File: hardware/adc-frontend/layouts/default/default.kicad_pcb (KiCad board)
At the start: 2 copper layers, 0 parts

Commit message: main.ato改修完了: オフラインato buildでPCB/BOM/ネットリスト生成成功
atopile部品API停止下で、EasyEDA取り込み部品を使い完全オフラインで
ato buildを通した。成果物: default.kicad_pcb(104フットプリント/612ネット)、
default.bom.csv(LCSC番号付き発注可能BOM)。

- parts/_mech/mech.ato: 手実装機構部品(ヘッダ2x15/1x4・ソルダージャンパ・
  TOSLINK PLR135)をフットプリント同居ディレクトリに配置し is_atomic_part +
  has_part_removed(DNP: 基板にFPは載るがJLC発注除外)で定義。自作footprint/symbol生成
- コネクタ(usbc/jack)のmanufacturer不一致修正
- EsdArray4をROHM EMZT6.8ET2R(6ピンA-Common Quad)へ

既知の残課題(製造前): (1)pinoutドキュメント生成はMagJack等のシンボル/パッド
不一致で失敗(netlist/PCBは生成済み)。(2)コネクタ類の仮ピン番号は実部品/EXT基板と
要照合。(3)ESD共通ノード位置(pin2/5)をROHMデータシートで要確認。(4)BOM値表示が
シンボリック({ℝ+}F)だがLCSC番号で部品は確定。

Co-Authored-By: Claude Fable 5 <noreply@anthropic.com>
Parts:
- added C1: {ℝ+}F, SAMSUNG_CL10A105KB8NNNC:C0603, F.Cu at (720.0, 0.00)
- added C10: {ℝ+}F, SAMSUNG_CL05B104KO5NNNC:C0402, F.Cu at (840.0, 0.00)
- added C11: {ℝ+}F, SAMSUNG_CL05B104KO5NNNC:C0402, F.Cu at (850.0, 0.00)
- added C12: {ℝ+}F, SAMSUNG_CL05B104KO5NNNC:C0402, F.Cu at (860.0, 0.00)
- added C13: {ℝ+}F, SAMSUNG_CL21A106KAYNNNE:C0805, F.Cu at (700.0, 0.00)
- added C14: {ℝ+}F, SAMSUNG_CL05B104KO5NNNC:C0402, F.Cu at (470.0, 0.00)
- added C15: {ℝ+}F, SAMSUNG_CL05B104KO5NNNC:C0402, F.Cu at (490.0, 0.00)
- added C16: {ℝ+}F, FH_0402B472K500NT:C0402, F.Cu at (500.0, 0.00)
- added C17: {ℝ+}F, SAMSUNG_CL05B104KO5NNNC:C0402, F.Cu at (510.0, 0.00)
- added C18: {ℝ+}F, FH_0402B102K500NT:C0402, F.Cu at (430.0, 0.00)
- added C19: {ℝ+}F, SAMSUNG_CL05B104KO5NNNC:C0402, F.Cu at (900.0, 0.00)
- added C2: {ℝ+}F, SAMSUNG_CL10A105KB8NNNC:C0603, F.Cu at (730.0, 0.00)
- added C20: {ℝ+}F, FH_0402B102K500NT:C0402, F.Cu at (460.0, 0.00)
- added C21: {ℝ+}F, SAMSUNG_CL05B104KO5NNNC:C0402, F.Cu at (680.0, 0.00)
- added C22: {ℝ+}F, SAMSUNG_CL05B104KO5NNNC:C0402, F.Cu at (410.0, 0.00)
- added C23: {ℝ+}F, SAMSUNG_CL05B104KO5NNNC:C0402, F.Cu at (390.0, 0.00)
- added C24: {ℝ+}F, SAMSUNG_CL05B104KO5NNNC:C0402, F.Cu at (370.0, 0.00)
- added C25: {ℝ+}F, SAMSUNG_CL05B104KO5NNNC:C0402, F.Cu at (220.0, 0.00)
- added C26: {ℝ+}F, SAMSUNG_CL05B104KO5NNNC:C0402, F.Cu at (230.0, 0.00)
- added C27: {ℝ+}F, SAMSUNG_CL05B104KO5NNNC:C0402, F.Cu at (240.0, 0.00)
- added C28: {ℝ+}F, SAMSUNG_CL05B104KO5NNNC:C0402, F.Cu at (250.0, 0.00)
- added C29: {ℝ+}F, SAMSUNG_CL05B104KO5NNNC:C0402, F.Cu at (260.0, 0.00)
- added C3: {ℝ+}F, SAMSUNG_CL21A106KAYNNNE:C0805, F.Cu at (740.0, 0.00)
- added C30: {ℝ+}F, SAMSUNG_CL05B104KO5NNNC:C0402, F.Cu at (270.0, 0.00)
- added C31: {ℝ+}F, SAMSUNG_CL05B104KO5NNNC:C0402, F.Cu at (280.0, 0.00)
- added C32: {ℝ+}F, SAMSUNG_CL05B104KO5NNNC:C0402, F.Cu at (290.0, 0.00)
- added C33: {ℝ+}F, SAMSUNG_CL05B104KO5NNNC:C0402, F.Cu at (300.0, 0.00)
- added C34: {ℝ+}F, SAMSUNG_CL05B104KO5NNNC:C0402, F.Cu at (310.0, 0.00)
- added C35: {ℝ+}F, SAMSUNG_CL05B104KO5NNNC:C0402, F.Cu at (320.0, 0.00)
- added C36: {ℝ+}F, SAMSUNG_CL05B104KO5NNNC:C0402, F.Cu at (330.0, 0.00)
- added C37: {ℝ+}F, SAMSUNG_CL05B104KO5NNNC:C0402, F.Cu at (340.0, 0.00)
- added C38: {ℝ+}F, SAMSUNG_CL05B104KO5NNNC:C0402, F.Cu at (350.0, 0.00)
- added C39: {ℝ+}F, SAMSUNG_CL05B104KO5NNNC:C0402, F.Cu at (940.0, 0.00)
- added C4: {ℝ+}F, SAMSUNG_CL05B104KO5NNNC:C0402, F.Cu at (750.0, 0.00)
- added C40: {ℝ+}F, SAMSUNG_CL05B104KO5NNNC:C0402, F.Cu at (950.0, 0.00)
- added C41: {ℝ+}F, YAGEO_CC1812KKX7RDBB472:C1812, F.Cu at (1020.0, 0.00)
- added C42: {ℝ+}F, YAGEO_CC1812KKX7RDBB472:C1812, F.Cu at (1030.0, 0.00)
- added C43: {ℝ+}F, SAMSUNG_CL05B104KO5NNNC:C0402, F.Cu at (980.0, 0.00)
- added C44: {ℝ+}F, SAMSUNG_CL05B104KO5NNNC:C0402, F.Cu at (990.0, 0.00)
- added C45: {ℝ+}F, SAMSUNG_CL05B104KO5NNNC:C0402, F.Cu at (1000.0, 0.00)
- added C46: {ℝ+}F, SAMSUNG_CL05B104KO5NNNC:C0402, F.Cu at (1010.0, 0.00)
- added C47: {ℝ+}F, SAMSUNG_CL05B103KB5NNNC:C0402, F.Cu at (520.0, 0.00)
- added C48: {ℝ+}F, SAMSUNG_CL05B103KB5NNNC:C0402, F.Cu at (530.0, 0.00)
- added C49: {ℝ+}F, SAMSUNG_CL05B103KB5NNNC:C0402, F.Cu at (540.0, 0.00)
- added C5: {ℝ+}F, SAMSUNG_CL05B104KO5NNNC:C0402, F.Cu at (760.0, 0.00)
- added C50: {ℝ+}F, SAMSUNG_CL05B103KB5NNNC:C0402, F.Cu at (550.0, 0.00)
- added C51: {ℝ+}F, SAMSUNG_CL05B103KB5NNNC:C0402, F.Cu at (560.0, 0.00)
- added C52: {ℝ+}F, SAMSUNG_CL05B103KB5NNNC:C0402, F.Cu at (570.0, 0.00)
- added C53: {ℝ+}F, SAMSUNG_CL05B103KB5NNNC:C0402, F.Cu at (580.0, 0.00)
- added C54: {ℝ+}F, FH_0402B102K500NT:C0402, F.Cu at (590.0, 0.00)
- added C55: {ℝ+}F, FH_0402B102K500NT:C0402, F.Cu at (600.0, 0.00)
- added C56: {ℝ+}F, SAMSUNG_CL21A106KAYNNNE:C0805, F.Cu at (110.0, 0.00)
- added C57: {ℝ+}F, SAMSUNG_CL21A106KAYNNNE:C0805, F.Cu at (120.0, 0.00)
- added C58: {ℝ+}F, SAMSUNG_CL21A106KAYNNNE:C0805, F.Cu at (130.0, 0.00)
- added C59: {ℝ+}F, SAMSUNG_CL21A106KAYNNNE:C0805, F.Cu at (140.0, 0.00)
- added C6: {ℝ+}F, SAMSUNG_CL05B104KO5NNNC:C0402, F.Cu at (770.0, 0.00)
- added C60: {ℝ+}F, SAMSUNG_CL21A106KAYNNNE:C0805, F.Cu at (150.0, 0.00)
- added C7: {ℝ+}F, SAMSUNG_CL10A105KB8NNNC:C0603, F.Cu at (810.0, 0.00)
- added C8: {ℝ+}F, SAMSUNG_CL10A105KB8NNNC:C0603, F.Cu at (820.0, 0.00)
- added C9: {ℝ+}F, SAMSUNG_CL21A106KAYNNNE:C0805, F.Cu at (830.0, 0.00)
- added D1: , ROHM_EMZT6_8ET2R:EMT6_L1.6-W1.2-P0.50-LS1.6-BL, F.Cu at (880.0, 0.00)
- added D2: , ROHM_EMZT6_8ET2R:EMT6_L1.6-W1.2-P0.50-LS1.6-BL, F.Cu at (420.0, 0.00)
- added D3: , ROHM_EMZT6_8ET2R:EMT6_L1.6-W1.2-P0.50-LS1.6-BL, F.Cu at (440.0, 0.00)
- added FB1: , TDK_MPZ1608S221ATA00:L0603, F.Cu at (690.0, 0.00)
- added FB2: , TDK_MPZ1608S221ATA00:L0603, F.Cu at (200.0, 0.00)
- added FB3: , TDK_MPZ1608S221ATA00:L0603, F.Cu at (210.0, 0.00)
- added J1: , _mech:Header_2x15_P2.54mm, F.Cu at (960.0, 0.00)
- added J10: , BOOMELE_VGA_002:D-SUB-TH_VGA-002, F.Cu at (10.0, 0.00)
- added J2: , HANRUN_HR911130A:RJ45-TH_HR911130A, F.Cu at (970.0, 0.00)
- added J3: , _mech:Header_2x15_P2.54mm, F.Cu at (650.0, 0.00)
- added J4: , _mech:Header_2x15_P2.54mm, F.Cu at (660.0, 0.00)
- added J5: , _mech:Header_1x4_P2.54mm, F.Cu at (910.0, 0.00)
- added J6: , UNKNOWN_PJ_327C_4A:AUDIO-SMD_PJ-327C-4A, F.Cu at (870.0, 0.00)
- added J7: , SHOU_HAN_DC005:DC-IN-TH_DC005, F.Cu at (40.0, 0.00)
- added J8: , _mech:PLR135_T10, F.Cu at (890.0, 0.00)
- added J9: , UNKNOWN_TYPE_C_31_M_12:USB-C_SMD-TYPE-C-31-M-12_1, F.Cu at (160.0, 0.00)
- added JP1: , _mech:SolderJumper_2, F.Cu at (780.0, 0.00)
- added JP2: , _mech:SolderJumper_2, F.Cu at (790.0, 0.00)
- added JP3: , _mech:SolderJumper_2, F.Cu at (190.0, 0.00)
- added R1: {ℝ+}Ω, UNI_ROYAL_0402WGF750JTCE:R0402, F.Cu at (400.0, 0.00)
- added R10: {ℝ+}Ω, UNI_ROYAL_0402WGF2201TCE:R0402, F.Cu at (620.0, 0.00)
- added R11: {ℝ+}Ω, UNI_ROYAL_0402WGF2200TCE:R0402, F.Cu at (450.0, 0.00)
- added R12: {ℝ+}Ω, FOJAN_FRC0402F62R0TS:R0402, F.Cu at (100.0, 0.00)
- added R13: {ℝ+}Ω, UNI_ROYAL_0402WGF1200TCE:R0402, F.Cu at (90.0, 0.00)
- added R2: {ℝ+}Ω, UNI_ROYAL_0402WGF750JTCE:R0402, F.Cu at (380.0, 0.00)
- added R3: {ℝ+}Ω, UNI_ROYAL_0402WGF750JTCE:R0402, F.Cu at (360.0, 0.00)
- added R4: {ℝ+}Ω, UNI_ROYAL_0402WGF5101TCE:R0402, F.Cu at (170.0, 0.00)
- added R5: {ℝ+}Ω, UNI_ROYAL_0402WGF5101TCE:R0402, F.Cu at (180.0, 0.00)
- added R6: {ℝ+}Ω, UNI_ROYAL_0402WGF1501TCE:R0402, F.Cu at (480.0, 0.00)
- added R7: {ℝ+}Ω, UNI_ROYAL_0402WGF2201TCE:R0402, F.Cu at (610.0, 0.00)
- added R8: {ℝ+}Ω, UNI_ROYAL_0402WGF2201TCE:R0402, F.Cu at (640.0, 0.00)
- added R9: {ℝ+}Ω, UNI_ROYAL_0402WGF2201TCE:R0402, F.Cu at (630.0, 0.00)
- added U1: , TI_PCM1808PWR:TSSOP-14_L5.0-W4.4-P0.65-LS6.4-BL, F.Cu at (710.0, 0.00)
- added U10: , TI_TVP7002PZP:HTQFP-100_L14.0-W14.0-P0.50-LS16.0-BL-EP6.2, F.Cu at (0.00, 0.00)
- added U2: , TI_PCM1808PWR:TSSOP-14_L5.0-W4.4-P0.65-LS6.4-BL, F.Cu at (800.0, 0.00)
- added U3: , TI_SN74LVC2G17DBVR:SOT-23-6_L2.9-W1.6-P0.95-LS2.8-BL, F.Cu at (20.0, 0.00)
- added U4: , MICROCHIP_24AA025E48_I_SN:SOIC-8_L4.9-W3.9-P1.27-LS6.0-BL, F.Cu at (920.0, 0.00)
- added U5: , MICROCHIP_24AA025E48_I_SN:SOIC-8_L4.9-W3.9-P1.27-LS6.0-BL, F.Cu at (930.0, 0.00)
- added U6: , DIODES_AZ1117H_ADJTRE1:SOT-223-3_L6.5-W3.4-P2.30-LS7.0-BR, F.Cu at (70.0, 0.00)
- added U7: , DIODES_AZ1117H_3_3TRE1:SOT-223-3_L6.5-W3.4-P2.30-LS7.0-BR, F.Cu at (60.0, 0.00)
- added U8: , TI_TLV70019DDCR:SOT-23-5_L2.9-W1.6-P0.95-LS2.8-BR, F.Cu at (80.0, 0.00)
- added U9: , DIODES_AZ1117H_3_3TRE1:SOT-223-3_L6.5-W3.4-P2.30-LS7.0-BR, F.Cu at (50.0, 0.00)
- added X1: , YXC_X322527MSB4SI:CRYSTAL-SMD_4P-L3.2-W2.5-BL-1, F.Cu at (30.0, 0.00)
- added X2: , YXC_OT2JI_111_12_288M:OSC-SMD_4P-L3.2-W2.5-BL, F.Cu at (670.0, 0.00)

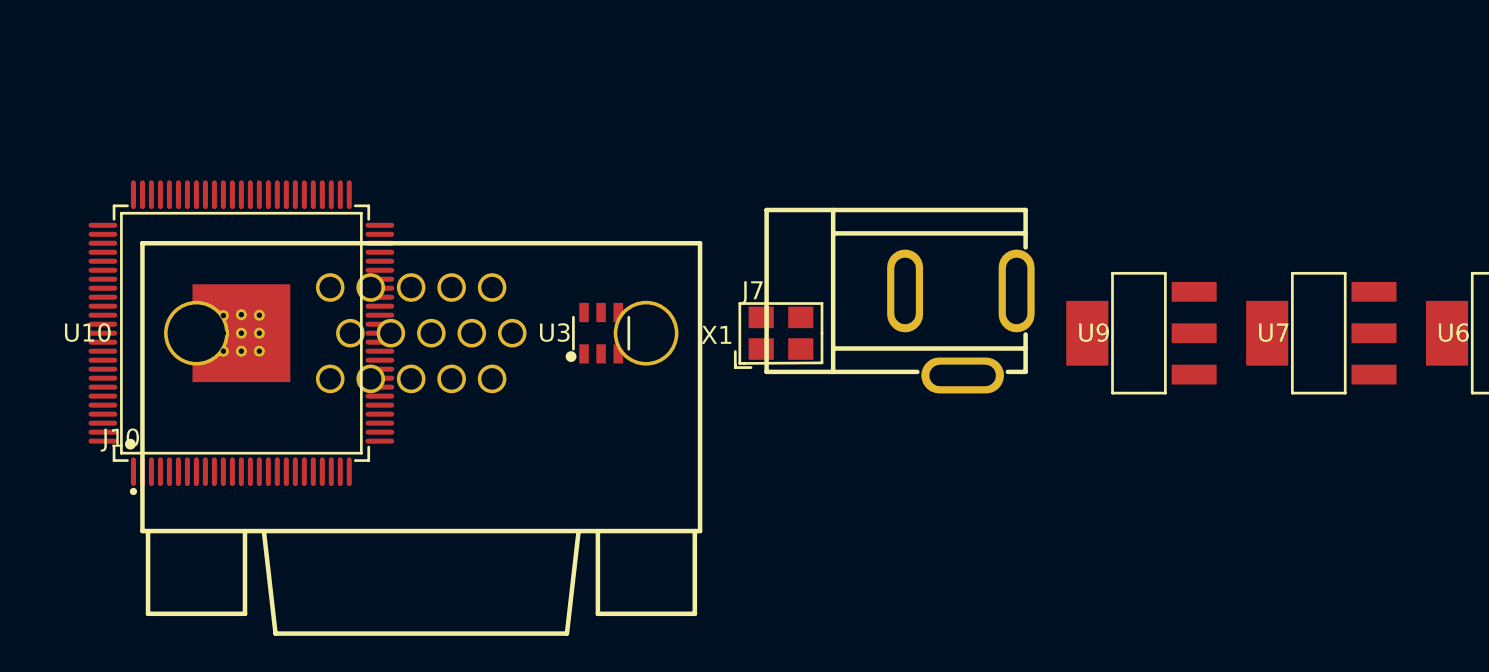
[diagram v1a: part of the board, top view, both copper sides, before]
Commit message: VGAを日本式D-SUB15(2列/X68000ピン配置)へ変更
3列HD-15(VGA-002)を廃し、2列DA-15メス CONNFLY DS1037-15FNAKT76-0CC
(C77836、EasyEDA取り込み)へ。X68000ピン配置(ohnaka提供):
1R 2RGND 3G 4GGND 5B 6BGND 7YS 8GND 9NC 10AudioL 11AudioR 12GND 13NC 14HSync 15VSync。
- RGB各GNDが交互配置。音声はpin10/11から取得(旧: VGA DDCピンの仮タップを廃止)
- 同期はpin14/15。YS(pin7)は未使用、pin9/13はNC
- App配線をr/g/b/audio_l/audio_r/hsync/vsync/*_gndへ再マッピング
オフラインato build確認(BOMにJ10=DS1037-15F)。VGA-002 partは未参照(残置)。

Co-Authored-By: Claude Fable 5 <noreply@anthropic.com>
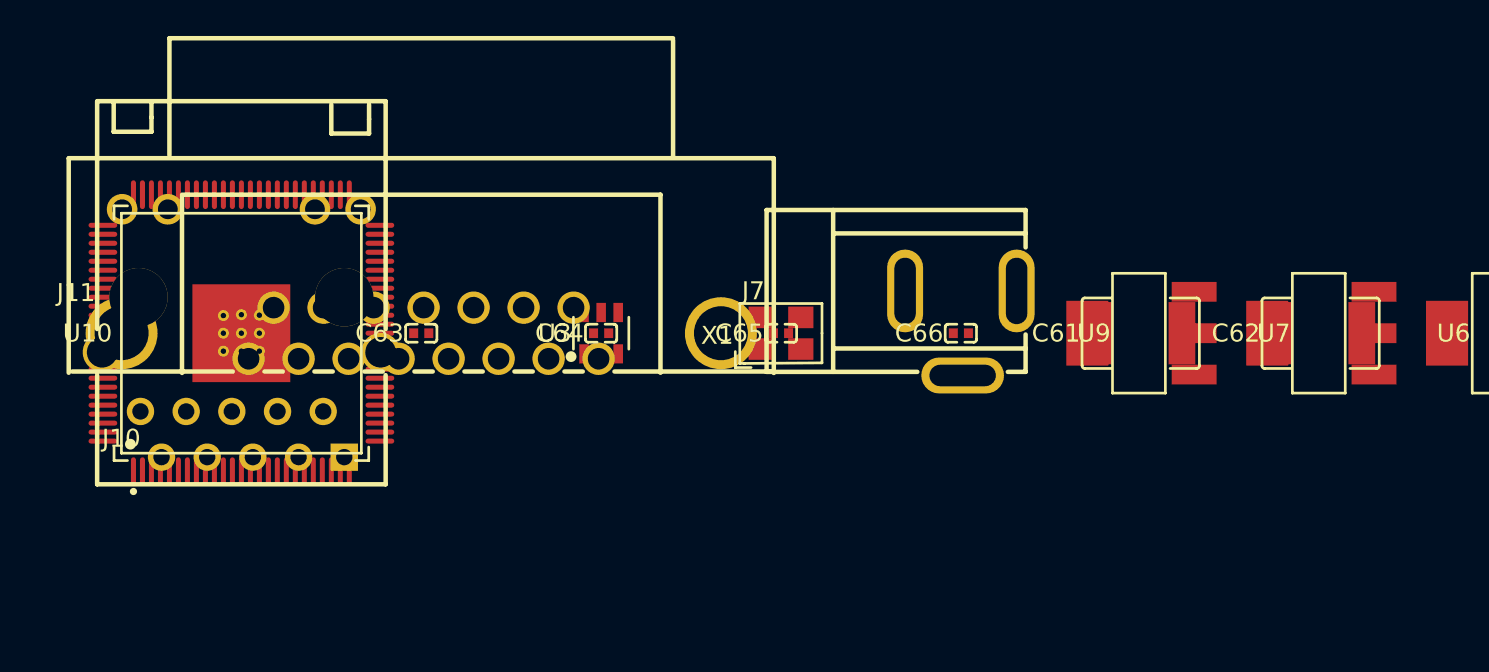
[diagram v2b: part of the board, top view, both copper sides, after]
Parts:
- added C61: {ℝ+}F, YAGEO_CC1812KKX7RDBB472:C1812, F.Cu at (50.0, 0.00)
- added C62: {ℝ+}F, YAGEO_CC1812KKX7RDBB472:C1812, F.Cu at (60.0, 0.00)
- added C63: {ℝ+}F, SAMSUNG_CL05B104KO5NNNC:C0402, F.Cu at (10.0, 0.00)
- added C64: {ℝ+}F, SAMSUNG_CL05B104KO5NNNC:C0402, F.Cu at (20.0, 0.00)
- added C65: {ℝ+}F, SAMSUNG_CL05B104KO5NNNC:C0402, F.Cu at (30.0, 0.00)
- added C66: {ℝ+}F, SAMSUNG_CL05B104KO5NNNC:C0402, F.Cu at (40.0, 0.00)
- added J11: , HANRUN_HR911130A:RJ45-TH_HR911130A, F.Cu at (0.00, 0.00)
- J10: footprint BOOMELE_VGA_002:D-SUB-TH_VGA-002 -> CONNFLY_DS1037_15FNAKT76_0CC:DSUB-TH_DS1037-15FNAKT74-0CC
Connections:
- J10 pad 1: c_ac-power-hv-1 -> (no net)
- J10 pad 10: gnd -> (no net)
- J10 pad 11: a-1 -> (no net)
- J10 pad 12: vga-sda -> (no net)
- J10 pad 13: 1 -> (no net)
- J10 pad 14: vsync -> (no net)
- J10 pad 15: vga-scl -> (no net)
- J10 pad 16: gnd -> (no net)
- J10 pad 2: c_sog3-power-hv -> (no net)
- J10 pad 3: c_ac-power-hv -> (no net)
- J10 pad 4: a -> (no net)
- J10 pad 5: gnd -> (no net)
- J10 pad 6: gnd -> (no net)
- J10 pad 7: gnd -> (no net)
- J10 pad 8: gnd -> (no net)
- J10 pad 9: key -> (no net)

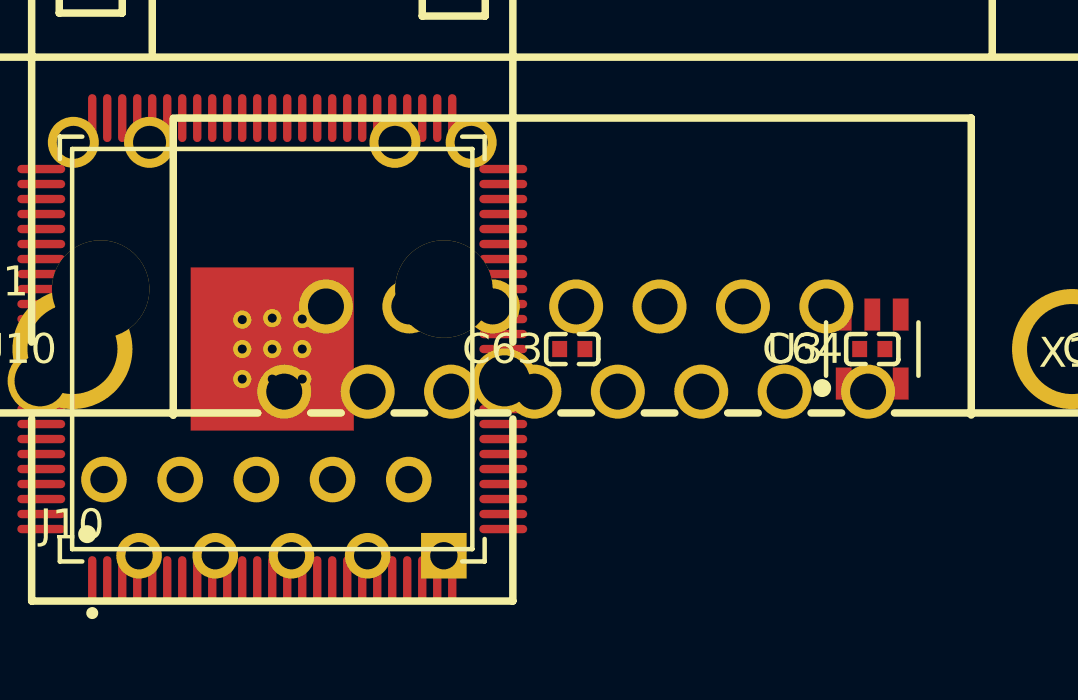
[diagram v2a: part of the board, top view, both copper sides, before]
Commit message: ArgusX接続用 2x8ボックスヘッダを追加(代替映像入力)
別プロジェクトArgusX(アナログRGBマトリクスセレクタ)の2x8汎用映像端子
(docs/design.md 3.1)と嵌合するボックスヘッダをRetroCastXに追加。
- ピン割当をArgusXに一致: 1R 2GND 3G 4GND 5B 6GND 7音声L 8音声R 9GND
  10H(TTL/CSYNC) 11V(TTL) 12GND 13+5V 14GND 15VBUS 16GND
- D-SUB15と同じ前段ノード(ESD+75Ω終端+ACカップリング/同期/音声)へ並列接続。
  使用は排他(同時に片方のみ)。電源13/15は両基板自己給電のため未接続
- 2x8シュラウド付きボックスヘッダのフットプリント+シンボルを自作(手実装/DNP)
オフラインato build確認(フットプリント111→112)。

Co-Authored-By: Claude Fable 5 <noreply@anthropic.com>
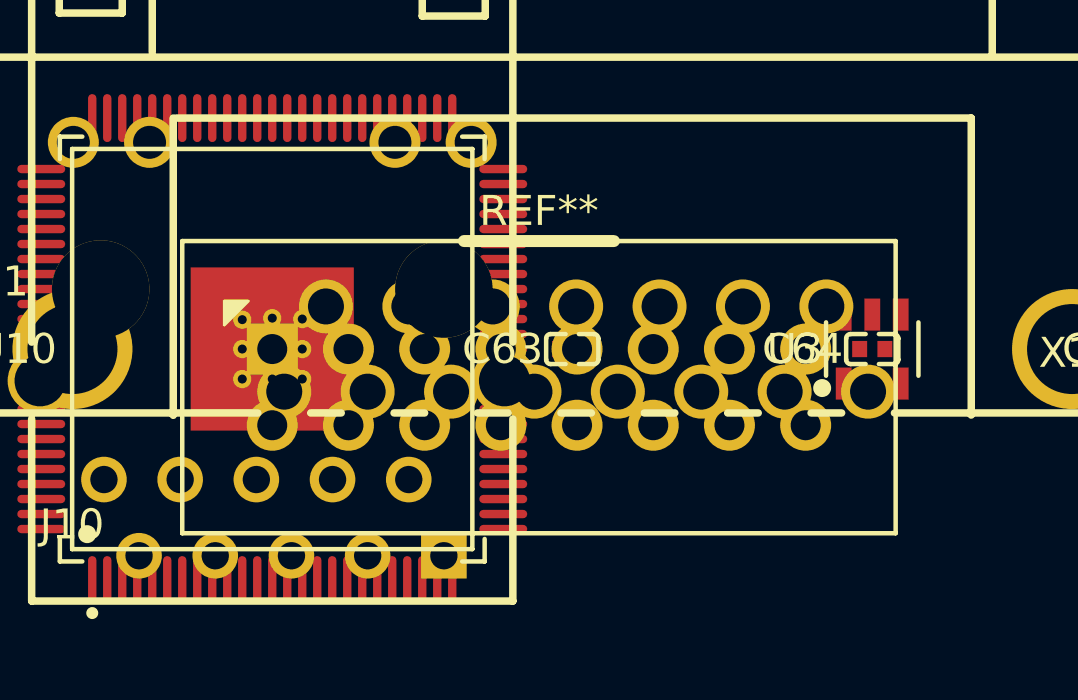
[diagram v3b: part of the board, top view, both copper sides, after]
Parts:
- added J12: , _mech:BoxHeader_2x8_P2.54mm, F.Cu at (0.00, 0.00)
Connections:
- C22 pad 1: c_ac-power-hv -> c_ac-power-hv-1
- C24 pad 1: c_ac-power-hv-1 -> c_ac-power-hv
- D2 pad 1: c_ac-power-hv-1 -> c_ac-power-hv
- D2 pad 4: c_ac-power-hv -> c_ac-power-hv-1
- D3 pad 1: 1 -> hsync
- J1 pad 1: eth.j8-1 -> 1
- J1 pad 19: eth.j8-1 -> 1
- J1 pad 2: eth.j8-1 -> 1
- J1 pad 20: eth.j8-1 -> 1
- J10 pad 1: (no net) -> c_ac-power-hv
- J10 pad 10: (no net) -> audio_l
- J10 pad 11: (no net) -> audio_r
- J10 pad 12: (no net) -> gnd
- J10 pad 14: (no net) -> hsync
- J10 pad 15: (no net) -> vsync
- J10 pad 16: (no net) -> gnd
- J10 pad 17: (no net) -> gnd
- J10 pad 2: (no net) -> gnd
- J10 pad 3: (no net) -> c_sog3-power-hv
- J10 pad 4: (no net) -> gnd
- J10 pad 5: (no net) -> c_ac-power-hv-1
- J10 pad 6: (no net) -> gnd
- J10 pad 7: (no net) -> ys
- J10 pad 8: (no net) -> gnd
- JP1 pad 1: a -> audio_l
- JP2 pad 1: a-1 -> audio_r
- R1 pad 1: c_ac-power-hv -> c_ac-power-hv-1
- R3 pad 1: c_ac-power-hv-1 -> c_ac-power-hv
- U3 pad 1: 1 -> hsync

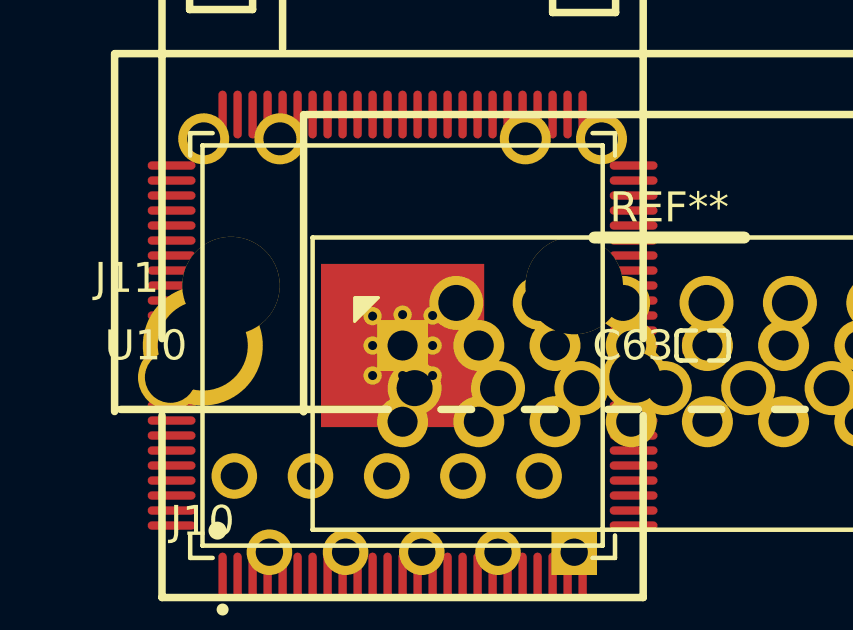
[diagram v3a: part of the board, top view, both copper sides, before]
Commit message: YS信号(D-SUB15 pin7)のテストパッドを追加
X68000のYSはスーパーインポーズ/イメージユニット関連のstatus信号らしい
(確定情報は未取得、capture用途では不要)。将来取り込む場合に備え、
1穴THテストパッド(Tp1Pad)へ引き出してNG時に配線可能にした。

実装メモ:
- コンポーネント名は標準ライブラリのTestPointと衝突するためTp1Padに改名
- テストパッドのフットプリントはfp_circleがあると"min() empty"で
  Updating PCBが落ちるため、パッドのみの最小構成にした
オフラインato build確認(フットプリント112→113、bom通過)。

Co-Authored-By: Claude Fable 5 <noreply@anthropic.com>
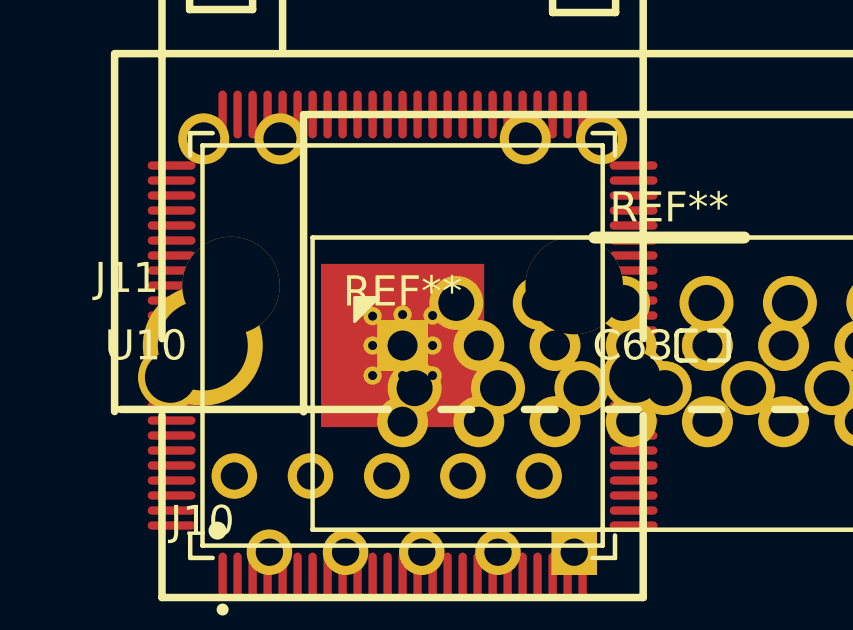
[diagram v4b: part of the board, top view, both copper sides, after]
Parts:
- added TP1: , _mech:TestPoint_TH1, F.Cu at (0.00, 0.00)
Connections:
- J10 pad 7: ys -> pad
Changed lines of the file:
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@@
 	(net 136 "audio_r")
 	(net 137 "audio_l")
-	(net 138 "ys")
+	(net 22 "pad")
 	(footprint "TI_TVP7002PZP:HTQFP-100_L14.0-W14.0-P0.50-LS16.0-BL-EP6.2"
 		(layer "F.Cu")
@@
 			(drill 1.199896)
 			(layers "*.Cu" "*.Mask")
-			(net 138 "ys")
+			(net 22 "pad")
 		)
 		(pad "8" thru_hole circle
@@
 		)
 		(pad "1" thru_hole rect
-			(at 0 0 0)
+			(at 0 0)
 			(size 1.7 1.7)
 			(drill 1)
@@
 		)
 		(pad "2" thru_hole oval
-			(at 0 2.54 0)
+			(at 0 2.54)
 			(size 1.7 1.7)
 			(drill 1)
@@
 		)
 		(pad "3" thru_hole oval
-			(at 2.54 0 0)
+			(at 2.54 0)
 			(size 1.7 1.7)
 			(drill 1)
@@
 		)
 		(pad "4" thru_hole oval
-			(at 2.54 2.54 0)
+			(at 2.54 2.54)
 			(size 1.7 1.7)
 			(drill 1)
@@
 		)
 		(pad "5" thru_hole oval
-			(at 5.08 0 0)
+			(at 5.08 0)
 			(size 1.7 1.7)
 			(drill 1)
@@
 		)
 		(pad "6" thru_hole oval
-			(at 5.08 2.54 0)
+			(at 5.08 2.54)
 			(size 1.7 1.7)
 			(drill 1)
@@
 		)
 		(pad "7" thru_hole oval
-			(at 7.62 0 0)
+			(at 7.62 0)
 			(size 1.7 1.7)
 			(drill 1)
@@
 		)
 		(pad "8" thru_hole oval
-			(at 7.62 2.54 0)
+			(at 7.62 2.54)
 			(size 1.7 1.7)
 			(drill 1)
@@
 		)
 		(pad "9" thru_hole oval
-			(at 10.16 0 0)
+			(at 10.16 0)
 			(size 1.7 1.7)
 			(drill 1)
@@
 		)
 		(pad "10" thru_hole oval
-			(at 10.16 2.54 0)
+			(at 10.16 2.54)
 			(size 1.7 1.7)
 			(drill 1)
@@
 		)
 		(pad "11" thru_hole oval
-			(at 12.7 0 0)
+			(at 12.7 0)
 			(size 1.7 1.7)
 			(drill 1)
@@
 		)
 		(pad "12" thru_hole oval
-			(at 12.7 2.54 0)
+			(at 12.7 2.54)
 			(size 1.7 1.7)
 			(drill 1)
@@
 		)
 		(pad "13" thru_hole oval
-			(at 15.24 0 0)
+			(at 15.24 0)
 			(size 1.7 1.7)
 			(drill 1)
@@
 		)
 		(pad "14" thru_hole oval
-			(at 15.24 2.54 0)
+			(at 15.24 2.54)
 			(size 1.7 1.7)
 			(drill 1)
@@
 		)
 		(pad "15" thru_hole oval
-			(at 17.78 0 0)
+			(at 17.78 0)
 			(size 1.7 1.7)
 			(drill 1)
@@
 		)
 		(pad "16" thru_hole oval
-			(at 17.78 2.54 0)
+			(at 17.78 2.54)
 			(size 1.7 1.7)
 			(drill 1)
@@
 		)
 	)
+	(footprint "_mech:TestPoint_TH1"
+		(layer "F.Cu")
+		(at 0 0 0)
+		(descr "Single through-hole test point (probe/wire). Hand-use.")
+		(property "Reference" "TP1"
+			(at 0 0 0)
+			(layer "F.SilkS")
+			(hide yes)
+		)
+		(property "Value" ""
+			(at 0 0 0)
+			(layer "User.9")
+			(hide yes)
+		)
+		(property "atopile_address" "tp_ys"
+			(at 0 0 0)
+			(layer "User.9")
+			(hide yes)
+		)
+		(attr through_hole exclude_from_pos_files)
+		(fp_text reference "REF**"
+			(at 0 -1.8)
+			(layer "F.SilkS")
+			(effects
+				(font
+					(size 1 1)
+					(thickness 0.15)
+				)
+			)
+		)
+		(fp_text value "TP"
+			(at 0 1.8)
+			(layer "F.Fab")
+			(effects
+				(font
+					(size 1 1)
+					(thickness 0.15)
+				)
+			)
+		)
+		(pad "1" thru_hole circle
+			(at 0 0 0)
+			(size 1.6 1.6)
+			(drill 0.8)
+			(layers "*.Cu" "*.Mask")
+			(net 22 "pad")
+		)
+	)
